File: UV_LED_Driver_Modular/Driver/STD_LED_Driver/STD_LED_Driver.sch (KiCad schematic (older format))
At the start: 1 part, among them J1 Conn_02x06_Odd_Even

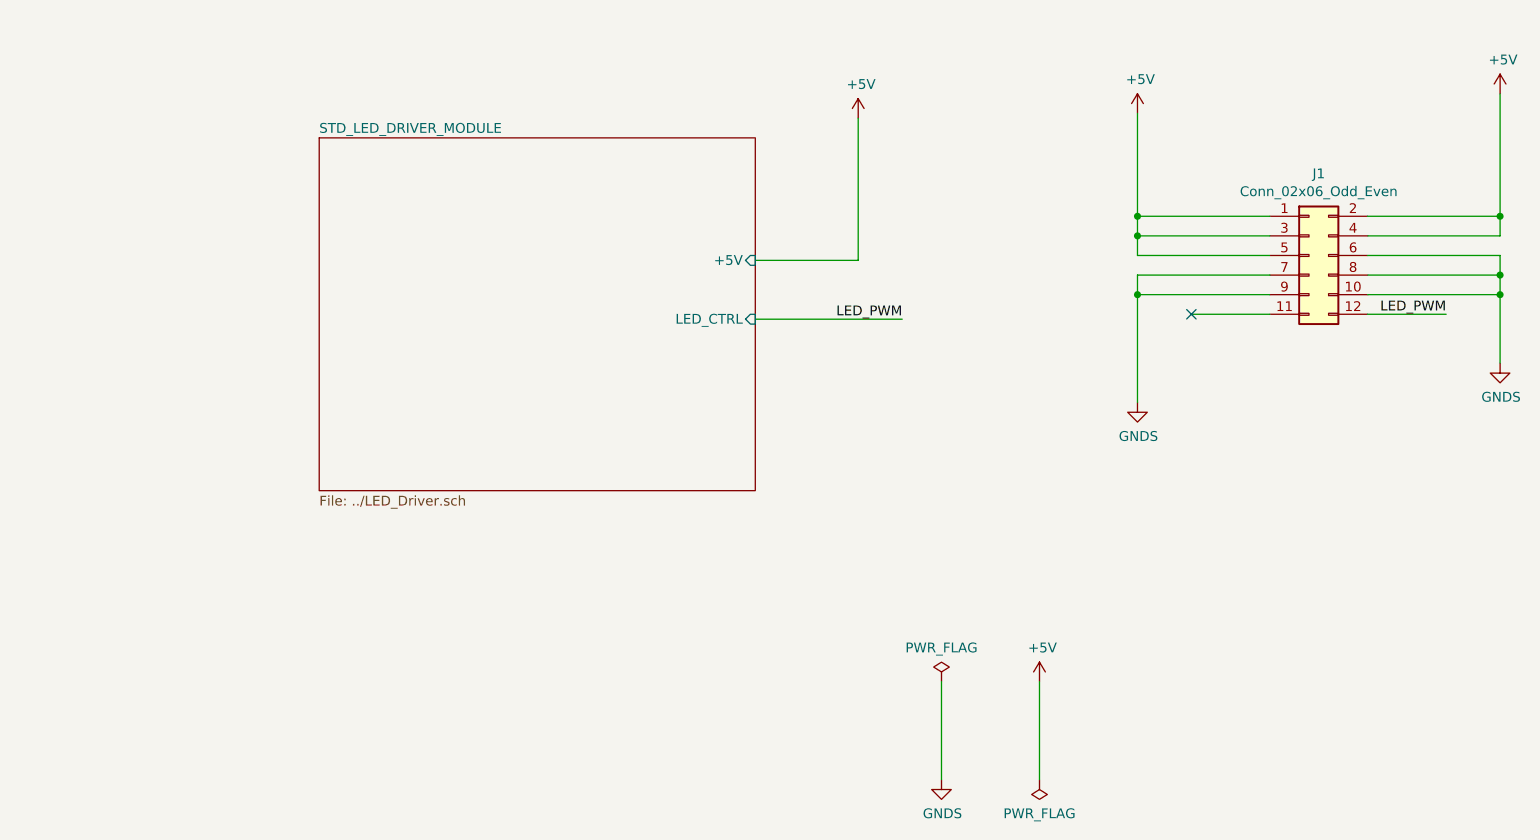
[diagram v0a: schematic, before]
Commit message: Changed TO225 NPN (MJE340) to SOT223 NPN (PZT2222A)
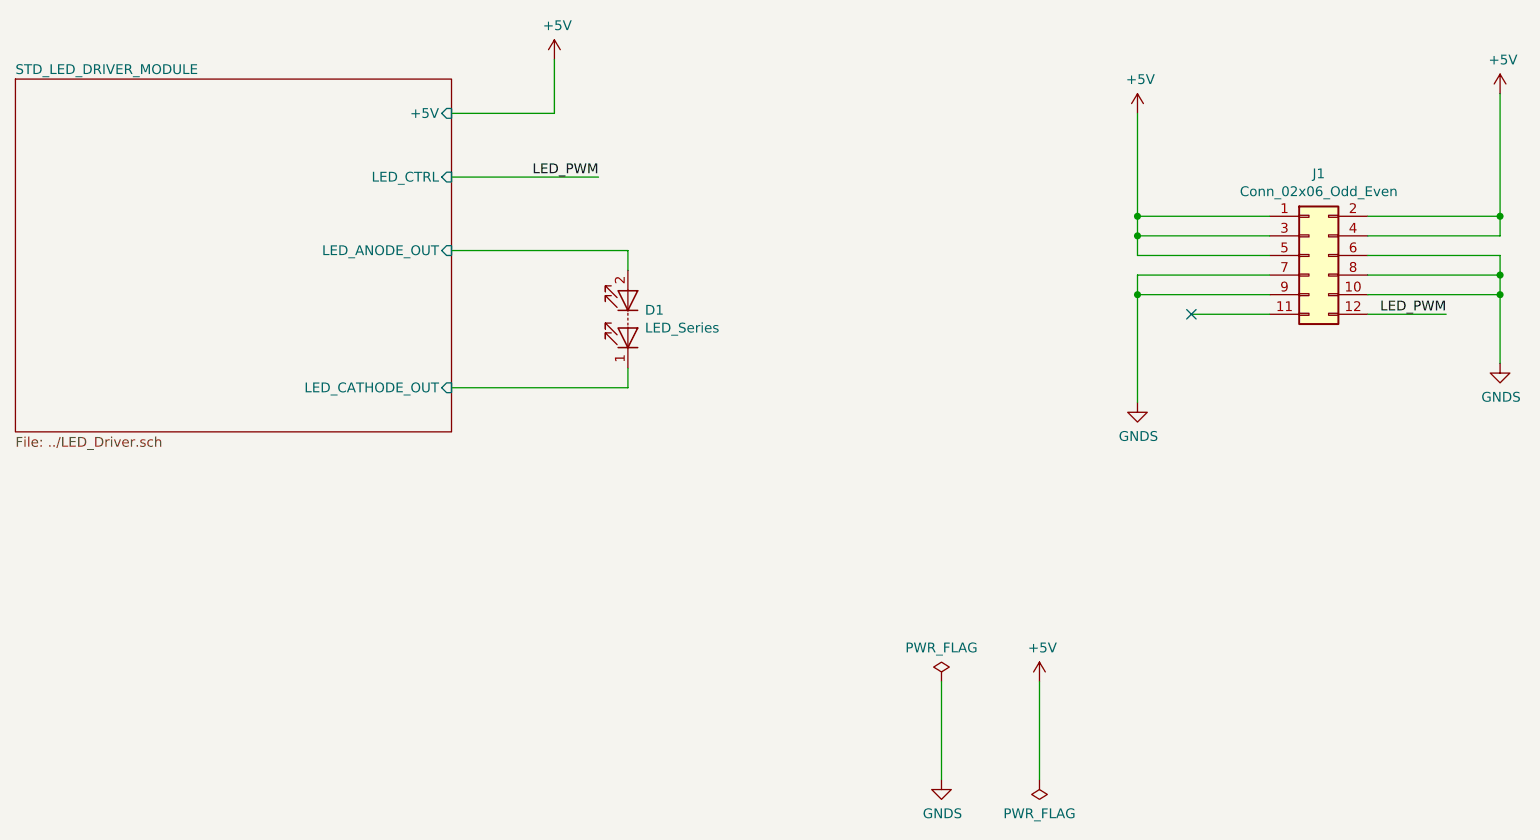
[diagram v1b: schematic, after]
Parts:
- added D1: LED_Series, Connector_Molex_MiniFitJnrExtra:Molex_Mini-Fit_Jr_5569-06A2_2x03_P4.20mm_Horizontal, symbol Device:LED_Series
- J1: footprint (none) -> Connector_IDC:IDC-Header_2x06_P2.54mm_Vertical
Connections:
- new net STD_LED_DRIVER_MODULE/LED_ANODE_OUT: D1.2 (A)
- new net STD_LED_DRIVER_MODULE/LED_CATHODE_OUT: D1.1 (K)
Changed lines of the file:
@@
 $EndDescr
 $Sheet
-S 3900 2650 2225 1800
+S 2350 2350 2225 1800
 U 5EA4121D
 F0 "STD_LED_DRIVER_MODULE" 50
 F1 "../LED_Driver.sch" 50
-F2 "+5V" I R 6125 3275 50
-F3 "LED_CTRL" I R 6125 3575 50
+F2 "+5V" I R 4575 2525 50
+F3 "LED_CTRL" I R 4575 2850 50
+F4 "LED_ANODE_OUT" I R 4575 3225 50
+F5 "LED_CATHODE_OUT" I R 4575 3925 50
 $EndSheet
 Wire Wire Line
-	6125 3275 6650 3275
-Wire Wire Line
-	6650 3275 6650 2550
+	4575 2525 5100 2525
+Wire Wire Line
+	5100 2525 5100 2250
 $Comp
 L power:+5V #PWR01
 U 1 1 5EA41716
-P 6650 2550
-F 0 "#PWR01" H 6650 2400 50  0001 C CNN
-F 1 "+5V" H 6665 2723 50  0000 C CNN
-F 2 "" H 6650 2550 50  0001 C CNN
-F 3 "" H 6650 2550 50  0001 C CNN
-	1    6650 2550
-	1    0    0    -1
-$EndComp
-Wire Wire Line
-	6125 3575 6875 3575
-Text Label 6875 3575 2    50   ~ 0
+P 5100 2250
+F 0 "#PWR01" H 5100 2100 50  0001 C CNN
+F 1 "+5V" H 5115 2423 50  0000 C CNN
+F 2 "" H 5100 2250 50  0001 C CNN
+F 3 "" H 5100 2250 50  0001 C CNN
+	1    5100 2250
+	1    0    0    -1
+$EndComp
+Wire Wire Line
+	4575 2850 5325 2850
+Text Label 5325 2850 2    50   ~ 0
 LED_PWM
 $Comp
@@
 F 0 "J1" H 9000 3667 50  0000 C CNN
 F 1 "Conn_02x06_Odd_Even" H 9000 3576 50  0000 C CNN
-F 2 "" H 8950 3250 50  0001 C CNN
+F 2 "Connector_IDC:IDC-Header_2x06_P2.54mm_Vertical" H 8950 3250 50  0001 C CNN
 F 3 "~" H 8950 3250 50  0001 C CNN
 	1    8950 3250
@@
 Wire Wire Line
 	7075 5925 7075 5425
+Wire Wire Line
+	4575 3225 5475 3225
+Wire Wire Line
+	4575 3925 5475 3925
+$Comp
+L Device:LED_Series D1
+U 1 1 5EA467FF
+P 5475 3575
+F 0 "D1" V 5521 3488 50  0000 R CNN
+F 1 "LED_Series" V 5430 3488 50  0000 R CNN
+F 2 "Connector_Molex_MiniFitJnrExtra:Molex_Mini-Fit_Jr_5569-06A2_2x03_P4.20mm_Horizontal" H 5375 3575 50  0001 C CNN
+F 3 "~" H 5375 3575 50  0001 C CNN
+	1    5475 3575
+	0    -1   -1   0
+$EndComp
+Wire Wire Line
+	5475 3325 5475 3225
+Wire Wire Line
+	5475 3825 5475 3925
 $EndSCHEMATC
